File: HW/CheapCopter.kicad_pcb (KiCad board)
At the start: 2 copper layers, 52 x 120.1 mm, 17 parts, among them M1 3-5V, M2 3-5V, M7 3-5V, M8 3-5V, U1 ESP32-WROOM-32, U2 PinHeader_1x08_P2.54mm_Vertic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, U3 L293D, U4 L293D, U5 L7805

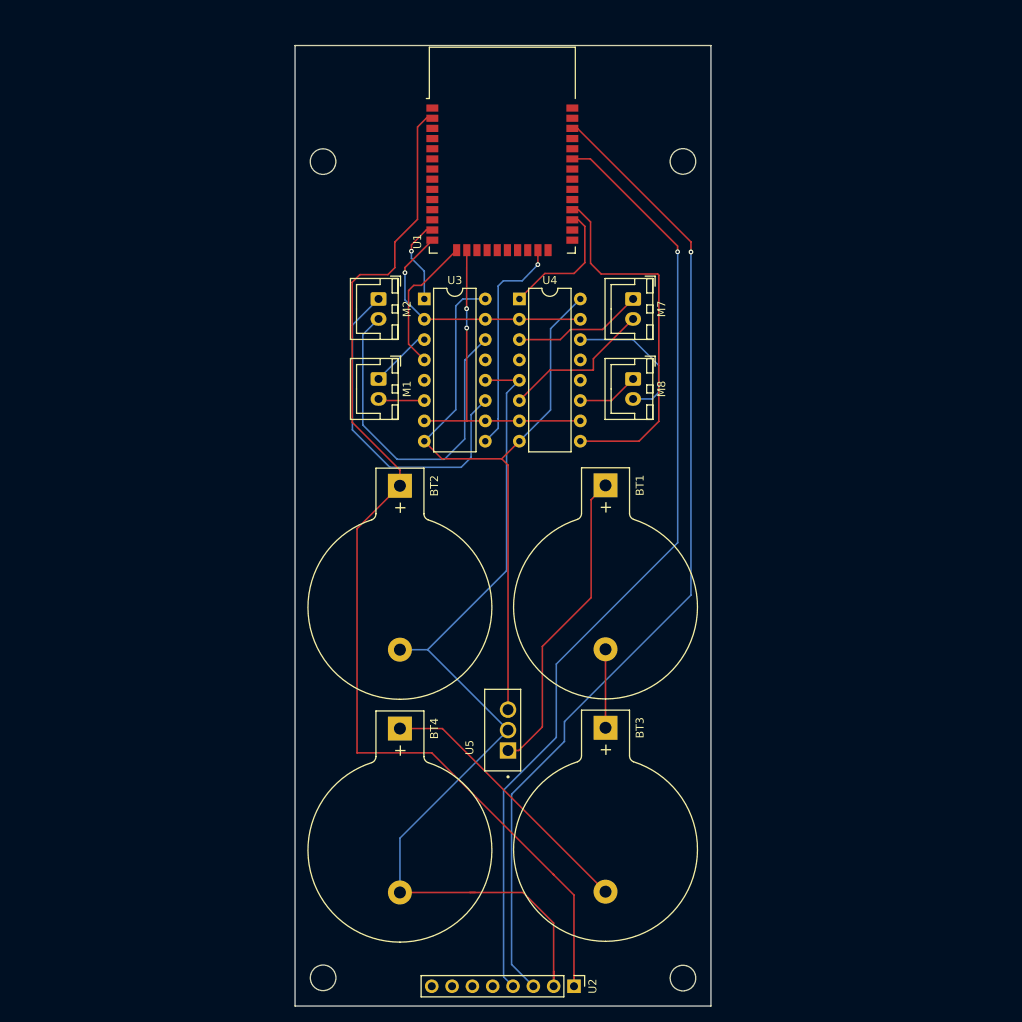
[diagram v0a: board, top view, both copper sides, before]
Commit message: First code
Added code for WiFi AP, OTA and basic wireless controlling
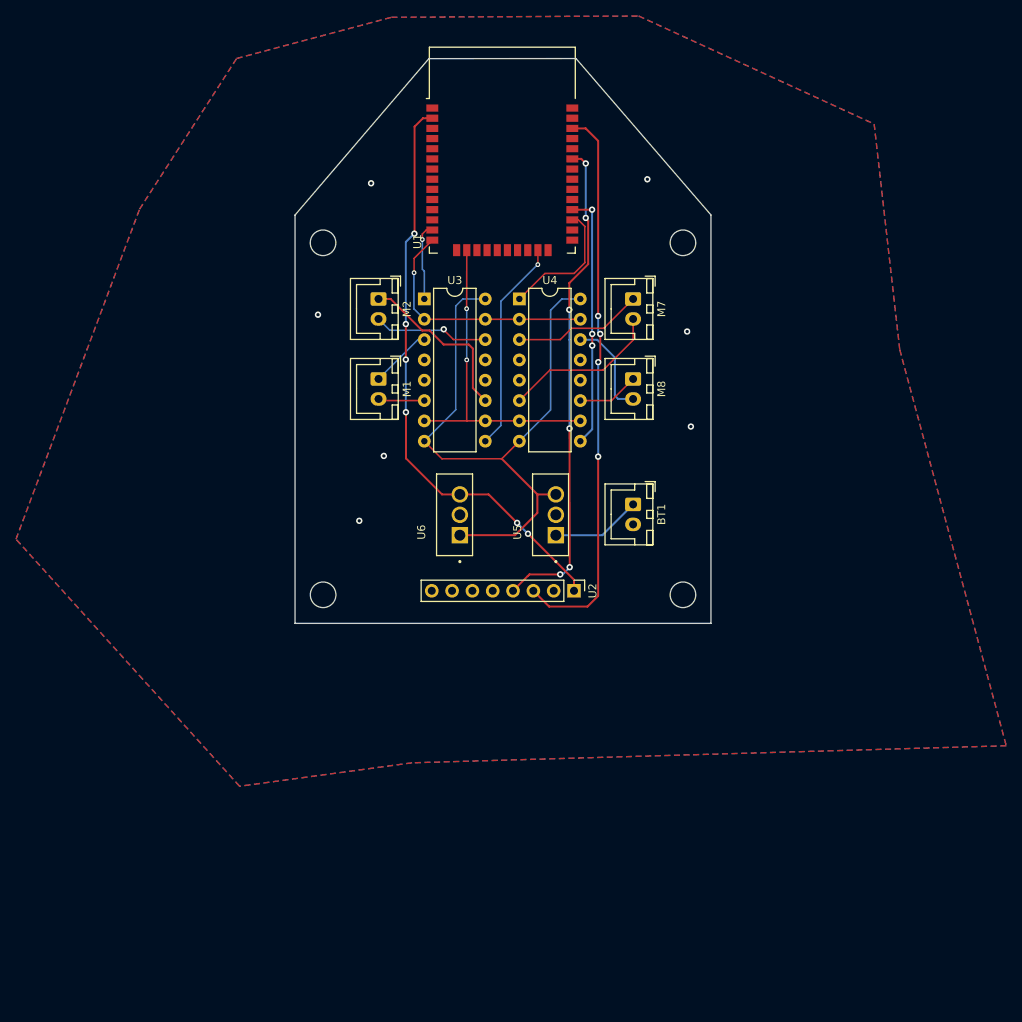
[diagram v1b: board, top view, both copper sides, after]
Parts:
- removed BT2, BT3, BT4: 3V, Battery:BatteryHolder_Keystone_103_1x20mm
- added U5: L7805, Transformer_THT:TO255P1020X450X2000-3, F.Cu at (149.0, 98.0)
- BT1: value 3V -> (none); footprint Battery:BatteryHolder_Keystone_103_1x20mm -> Connector_JST:JST_XH_B2B-XH-A_1x02_P2.50mm_Vertical
- moved U2 49.4 mm to (151.9, 107.5)
- moved ? 47.9 mm to (165.6, 108.0)
- moved ? 47.9 mm to (120.6, 108.0)
- moved U6 27.6 mm to (137.0, 98.0)
- moved ? 10.2 mm to (165.6, 64.0)
- moved ? 10.1 mm to (120.6, 64.0)
- moved BT1 4.19 mm to (159.3, 96.7)
- renumbered U5 to U6
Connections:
- BT1 pad 1: Net-(BT4-+) -> +7.4V
- BT1 pad 2: Net-(BT2-+) -> GND
- U3 pad 13: unconnected-GND -> GND
- U3 pad 5: unconnected-GND -> GND
- U4 pad 12: unconnected-GND -> GND
- U4 pad 13: unconnected-GND -> GND
- U4 pad 4: unconnected-GND -> GND
- U6 pad 1: Net-(BT4-+) -> +5V
- U6 pad 3: +5V -> +3V3
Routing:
- net GND: track 134.5 -> 0.28 mm, vias 0 -> 7
- net +3V3: track 137.1 -> 74.7 mm, vias 0 -> 6
- net Net-(U1-IO21): track 119.7 -> 62.4 mm, vias 1 -> 6
- net Net-(U1-IO22): track 124.2 -> 71.4 mm, vias 1 -> 4
- net Net-(BT4-+): track 39.0 -> 0.00 mm
- net Net-(BT3-+): track 34.1 -> 0.00 mm
- net Net-(M6--): track 43.1 -> 14.7 mm, vias 0 -> 1
- net Net-(M6-+): track 42.8 -> 21.5 mm
- net Net-(U1-IO17): track 46.4 -> 32.0 mm, vias 0 -> 3
- net +7.4V: track 0.00 -> 11.3 mm
- net Net-(BT2-+): track 10.1 -> 0.00 mm
- net +5V: track 88.9 -> 80.3 mm
- net Net-(M8--): track 18.0 -> 12.5 mm
- net Net-(U1-IO15): track 28.1 -> 26.8 mm
- net Net-(U1-IO14): track 10.8 -> 9.68 mm
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- added copper zone on B.Cu, net GND
- added copper zone on F.Cu, net GND
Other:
- board size 52 x 120.1 mm -> 52 x 70.6 mm
